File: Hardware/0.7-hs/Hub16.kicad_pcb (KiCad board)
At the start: 2 copper layers, 89 x 100 mm, 132 parts, among them J1 USB_C_Receptacle_USB2.0, J2 AVR-ISP-6, J3 USB_C_Receptacle_USB2.0, J4 USB_C_Receptacle_USB2.0, J5 USB_C_Receptacle_USB2.0, K1 KEYSW, K11 KEYSW, K12 KEYSW, K13 KEYSW, K14 KEYSW, K16 KEYSW, K17 KEYSW, K18 KEYSW, K19 KEYSW, K2 KEYSW, K3 KEYSW, K4 KEYSW, K6 KEYSW, K7 KEYSW, K8 KEYSW, K9 KEYSW, SW1 KMR2, SW2 Rotary_Encoder_Switch, SW3 Rotary_Encoder_Switch, U1 USBLC6-2SC6, U2 ATMEGA32U4, U3 CY7C65632-28LTXCT, U4 USBLC6-2SC6, U5 USBLC6-2SC6, U6 USBLC6-2SC6, Y1 16MHz, Y2 12MHz

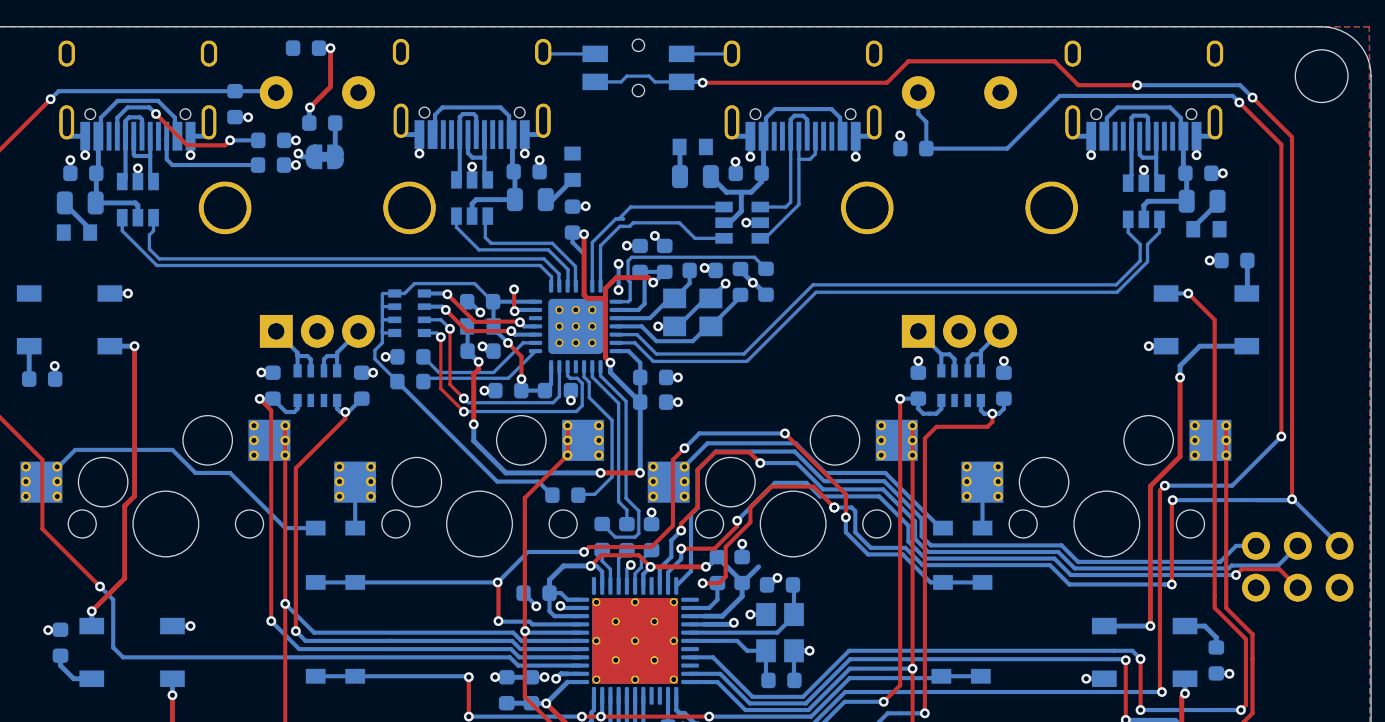
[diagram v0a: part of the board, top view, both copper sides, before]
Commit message: clean up usb routing + pdn check
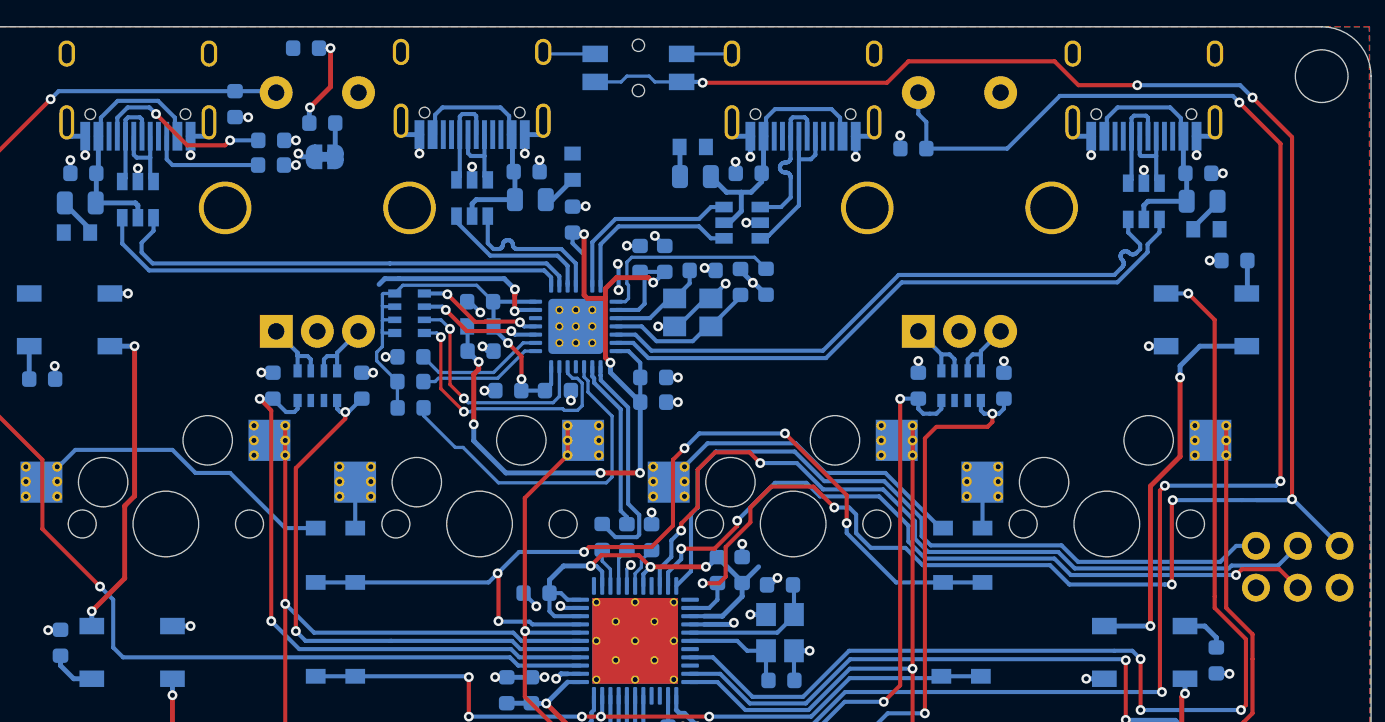
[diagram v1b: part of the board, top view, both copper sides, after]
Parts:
- moved R10 10.8 mm to (78.2, 62.1)
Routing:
- net Net-(R10-Pad1): track 9.89 -> 21.2 mm
- net +3V3: track 40.5 -> 29.7 mm
- net +5V: track 75.9 -> 84.6 mm
- net /ENC_2_SW: track 101.4 -> 102.9 mm
- net /USB Hub/UP_USB_P: track 28.3 -> 29.0 mm
- net /USB Hub/D1_D+: track 8.84 -> 9.55 mm
- net /USB Hub/CON2_D-: track 9.19 -> 9.90 mm
- net /row1: track 59.1 -> 59.7 mm
- net /USB Hub/D3_D+: track 38.1 -> 37.6 mm
- net /nRST: track 125.2 -> 125.1 mm, vias 9 -> 8
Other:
- net class USB added: clearance 0.15, trace_width 0.25, via_dia 0.6, via_drill 0.3

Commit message: update board
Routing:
- net GND: track 104.1 -> 102.5 mm, vias 78 -> 76
- net Net-(R14-Pad1): track 11.9 -> 10.6 mm, vias 0 -> 2
- net +3.3VA: track 53.7 -> 54.7 mm

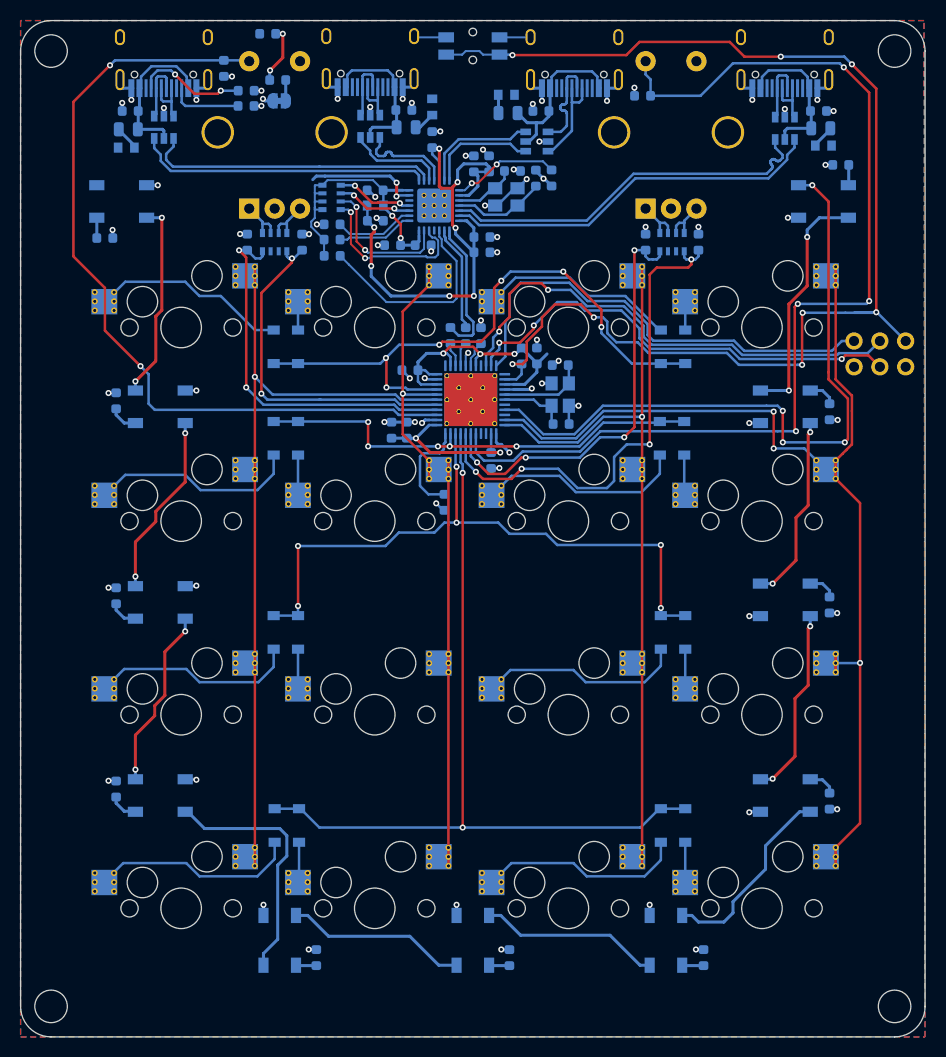
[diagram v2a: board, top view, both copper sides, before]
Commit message: fix v0.5 bom + release prototypes
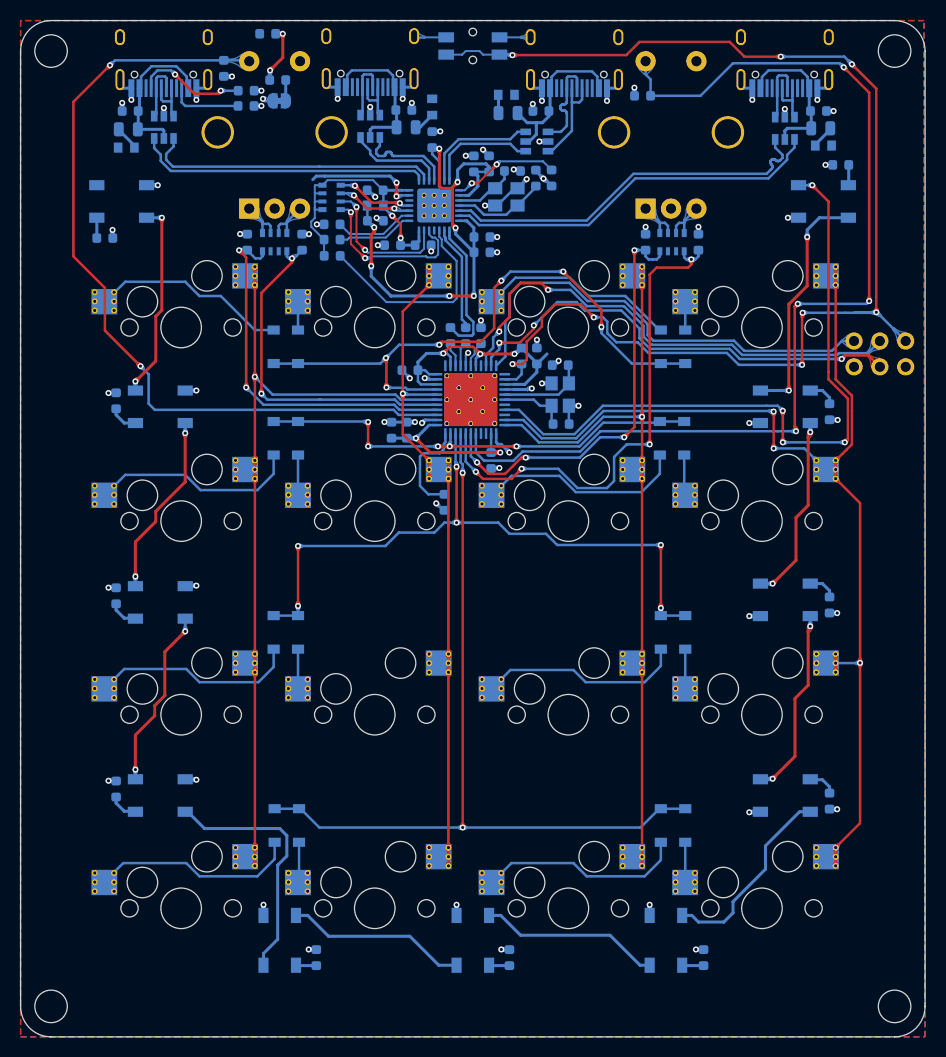
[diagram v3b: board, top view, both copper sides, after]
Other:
- board text added: "JLCJLCJLC"

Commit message: update sockets with courtyard
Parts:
- C17, C18, C2, C3: value 22p -> 15p
- D11, D12, D13, D14, D17, D18, D19, D20, D24, D25, D26, D27, D5, D6, D7, D8: value D -> 1N4148
- K1, K11, K12, K13, K14, K16, K17, K18, K19, K2, K3, K4, K6, K7, K8, K9: value KEYSW -> Kailh Hotswap Socket
- SW1: value KMR2 -> EVQPUL
- SW2, SW3: value Rotary_Encoder_Switch -> EC11 Encoder

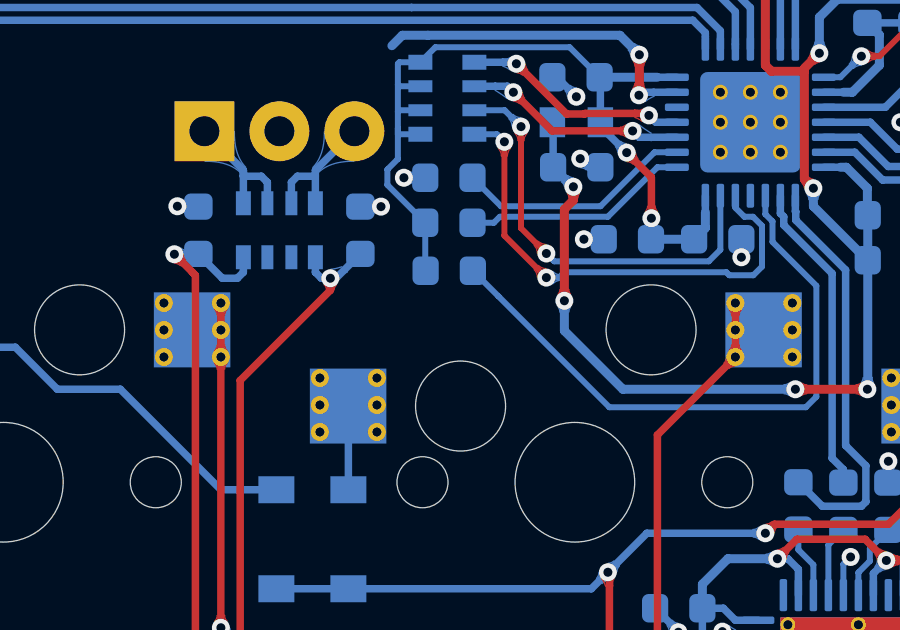
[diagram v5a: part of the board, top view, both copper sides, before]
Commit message: move res with HS interference
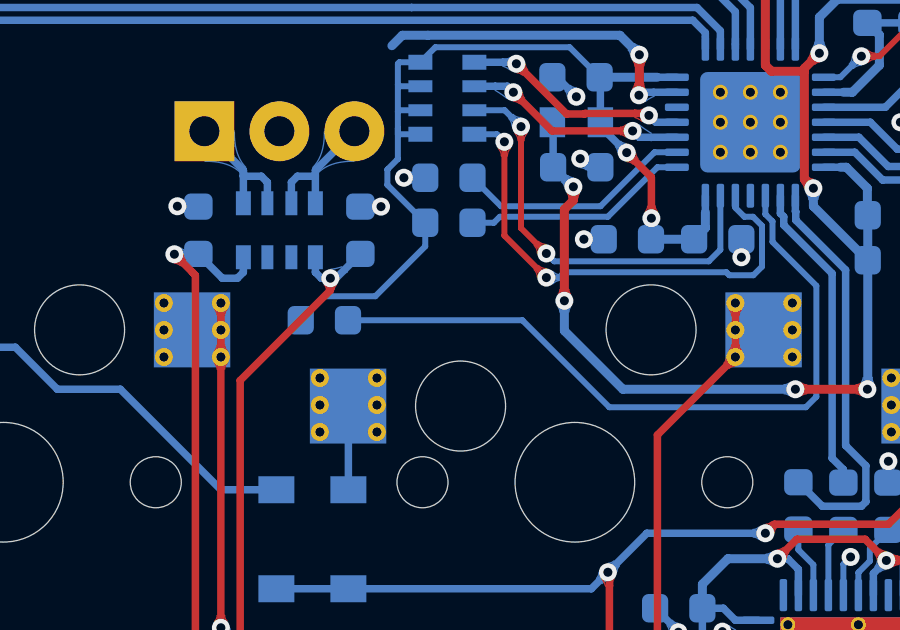
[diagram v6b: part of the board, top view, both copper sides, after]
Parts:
- moved R10 4.48 mm to (74.0, 63.8)
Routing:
- net +3V3: track 29.7 -> 34.0 mm
- net Net-(R10-Pad1): track 20.9 -> 24.4 mm
